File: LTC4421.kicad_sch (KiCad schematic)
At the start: 59 parts, among them U2 LTC4421CG-PBF, U3 74LVC2G07GV,125, U4 74LVC2G07GV,125, U5 74LVC2G07GV,125

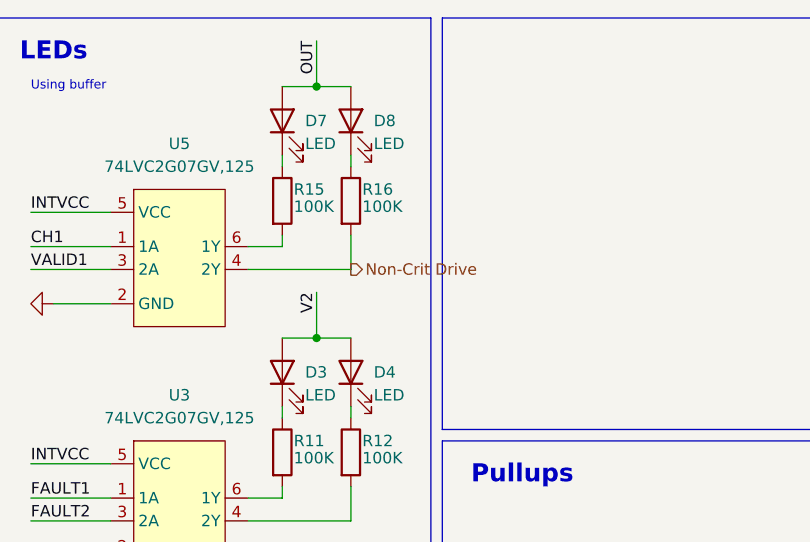
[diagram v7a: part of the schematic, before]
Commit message: fixes for IGN and non-crit
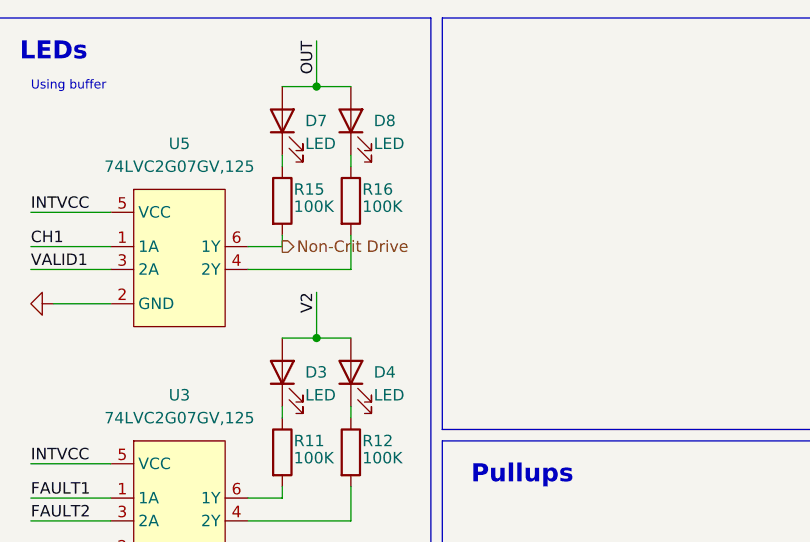
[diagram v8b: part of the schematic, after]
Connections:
- net Non-Crit Drive: now also R15.2, U5.6 (1Y); no longer R16.2, U5.4 (2Y)
- new net: R16.2, U5.4 (2Y)
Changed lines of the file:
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@@
 	(hierarchical_label "Non-Crit Drive"
 		(shape output)
-		(at 166.37 40.64 0)
+		(at 158.75 38.1 0)
 		(fields_autoplaced yes)
 		(effects
